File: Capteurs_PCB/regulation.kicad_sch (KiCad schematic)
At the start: 23 parts, among them U2 AZ1117-3.3

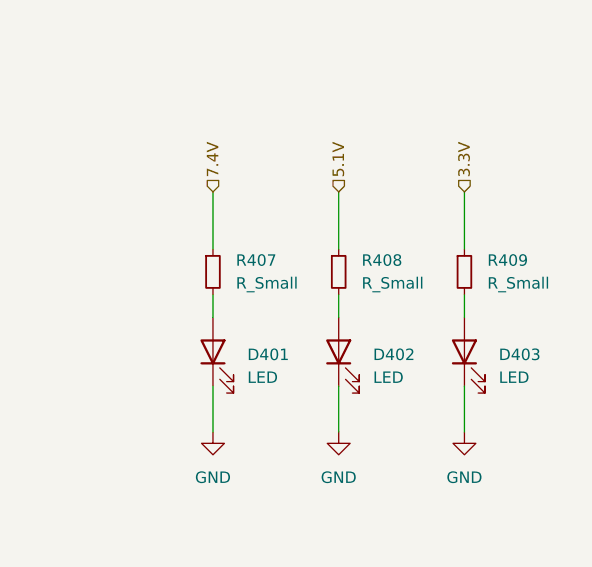
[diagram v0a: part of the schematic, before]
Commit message: Empreintes
A revoir car pas sur pour certaines + faire celles des composants modifiés
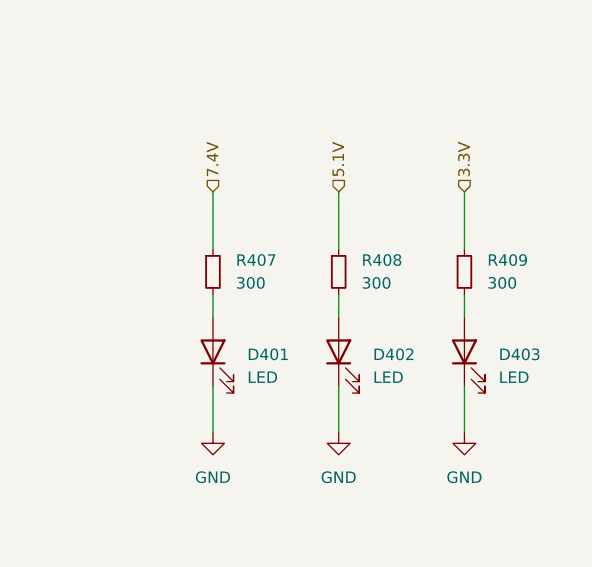
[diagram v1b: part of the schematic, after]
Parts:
- D401, D402, D403: footprint (none) -> LED_THT:LED_D5.0mm_Clear
- R1, R2, R401, R402, R403, R404: footprint (none) -> Resistor_SMD:R_0805_2012Metric
- R407, R408, R409: value R_Small -> 300; footprint (none) -> Resistor_SMD:R_0805_2012Metric
- U2: footprint (none) -> Package_TO_SOT_THT:TO-220-3_Vertical
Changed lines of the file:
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@@
       (effects (font (size 1.27 1.27)))
     )
-    (property "Footprint" "" (at 69.85 113.03 0)
+    (property "Footprint" "Resistor_SMD:R_0805_2012Metric" (at 69.85 113.03 0)
       (effects (font (size 1.27 1.27)) hide)
     )
@@
       (effects (font (size 1.27 1.27)) (justify left))
     )
-    (property "Footprint" "" (at 104.14 116.84 0)
+    (property "Footprint" "Resistor_SMD:R_0805_2012Metric" (at 104.14 116.84 0)
       (effects (font (size 1.27 1.27)) hide)
     )
@@
       (effects (font (size 1.27 1.27)) (justify right))
     )
-    (property "Footprint" "" (at 199.39 82.55 0)
+    (property "Footprint" "LED_THT:LED_D5.0mm_Clear" (at 199.39 82.55 0)
       (effects (font (size 1.27 1.27)) hide)
     )
@@
       (effects (font (size 1.27 1.27)) (justify right))
     )
-    (property "Footprint" "" (at 185.42 82.55 0)
+    (property "Footprint" "LED_THT:LED_D5.0mm_Clear" (at 185.42 82.55 0)
       (effects (font (size 1.27 1.27)) hide)
     )
@@
       (effects (font (size 1.27 1.27)) (justify left))
     )
-    (property "Value" "R_Small" (at 215.9 74.93 0)
-      (effects (font (size 1.27 1.27)) (justify left))
-    )
-    (property "Footprint" "" (at 213.36 73.66 0)
+    (property "Value" "300" (at 215.9 74.93 0)
+      (effects (font (size 1.27 1.27)) (justify left))
+    )
+    (property "Footprint" "Resistor_SMD:R_0805_2012Metric" (at 213.36 73.66 0)
       (effects (font (size 1.27 1.27)) hide)
     )
@@
       (effects (font (size 1.27 1.27)))
     )
-    (property "Footprint" "" (at 69.85 67.31 0)
+    (property "Footprint" "Resistor_SMD:R_0805_2012Metric" (at 69.85 67.31 0)
       (effects (font (size 1.27 1.27)) hide)
     )
@@
       (effects (font (size 1.27 1.27)) (justify left))
     )
-    (property "Value" "R_Small" (at 201.93 74.93 0)
-      (effects (font (size 1.27 1.27)) (justify left))
-    )
-    (property "Footprint" "" (at 199.39 73.66 0)
+    (property "Value" "300" (at 201.93 74.93 0)
+      (effects (font (size 1.27 1.27)) (justify left))
+    )
+    (property "Footprint" "Resistor_SMD:R_0805_2012Metric" (at 199.39 73.66 0)
       (effects (font (size 1.27 1.27)) hide)
     )
@@
       (effects (font (size 1.27 1.27)) (justify left))
     )
-    (property "Footprint" "" (at 104.14 109.22 0)
+    (property "Footprint" "Resistor_SMD:R_0805_2012Metric" (at 104.14 109.22 0)
       (effects (font (size 1.27 1.27)) hide)
     )
@@
       (effects (font (size 1.27 1.27)) (justify right))
     )
-    (property "Footprint" "" (at 213.36 82.55 0)
+    (property "Footprint" "LED_THT:LED_D5.0mm_Clear" (at 213.36 82.55 0)
       (effects (font (size 1.27 1.27)) hide)
     )
@@
       (effects (font (size 1.27 1.27)))
     )
-    (property "Footprint" "" (at 86.36 140.97 0)
+    (property "Footprint" "Package_TO_SOT_THT:TO-220-3_Vertical" (at 86.36 140.97 0)
       (effects (font (size 1.27 1.27) italic) hide)
     )
@@
       (effects (font (size 1.27 1.27)) (justify left))
     )
-    (property "Value" "R_Small" (at 187.96 74.93 0)
-      (effects (font (size 1.27 1.27)) (justify left))
-    )
-    (property "Footprint" "" (at 185.42 73.66 0)
+    (property "Value" "300" (at 187.96 74.93 0)
+      (effects (font (size 1.27 1.27)) (justify left))
+    )
+    (property "Footprint" "Resistor_SMD:R_0805_2012Metric" (at 185.42 73.66 0)
       (effects (font (size 1.27 1.27)) hide)
     )
@@
       (effects (font (size 1.27 1.27)) (justify left))
     )
-    (property "Footprint" "" (at 104.14 63.5 0)
+    (property "Footprint" "Resistor_SMD:R_0805_2012Metric" (at 104.14 63.5 0)
       (effects (font (size 1.27 1.27)) hide)
     )
@@
       (effects (font (size 1.27 1.27)) (justify left))
     )
-    (property "Footprint" "" (at 104.14 71.12 0)
-      (effects (font (size 1.27 1.27)) hide)
-    )
+    (property "Footprint" "Resistor_SMD:R_0805_2012Metric" (at 104.14 71.12 0)
+      (effects (font (size 1.27 1.27)) hide)
+    )

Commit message: Empreintes modifiées
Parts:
- C401, C405, C407, C408: footprint Capacitor_SMD:C_1206_3216Metric -> Capacitor_SMD:C_1206_3216Metric_Pad1.33x1.80mm_HandSolder
- R1, R2, R401, R402, R403, R404, R407, R408, R409: footprint Resistor_SMD:R_0805_2012Metric -> Resistor_SMD:R_0603_1608Metric_Pad0.98x0.95mm_HandSolder
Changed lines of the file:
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@@
       (effects (font (size 1.27 1.27)))
     )
-    (property "Footprint" "Resistor_SMD:R_0805_2012Metric" (at 69.85 113.03 0)
+    (property "Footprint" "Resistor_SMD:R_0603_1608Metric_Pad0.98x0.95mm_HandSolder" (at 69.85 113.03 0)
       (effects (font (size 1.27 1.27)) hide)
     )
@@
       (effects (font (size 1.27 1.27)) (justify left))
     )
-    (property "Footprint" "Resistor_SMD:R_0805_2012Metric" (at 104.14 116.84 0)
+    (property "Footprint" "Resistor_SMD:R_0603_1608Metric_Pad0.98x0.95mm_HandSolder" (at 104.14 116.84 0)
       (effects (font (size 1.27 1.27)) hide)
     )
@@
       (effects (font (size 1.27 1.27)))
     )
-    (property "Footprint" "Capacitor_SMD:C_1206_3216Metric" (at 69.85 69.85 0)
+    (property "Footprint" "Capacitor_SMD:C_1206_3216Metric_Pad1.33x1.80mm_HandSolder" (at 69.85 69.85 0)
       (effects (font (size 1.27 1.27)) hide)
     )
@@
       (effects (font (size 1.27 1.27)) (justify left))
     )
-    (property "Footprint" "Resistor_SMD:R_0805_2012Metric" (at 213.36 73.66 0)
+    (property "Footprint" "Resistor_SMD:R_0603_1608Metric_Pad0.98x0.95mm_HandSolder" (at 213.36 73.66 0)
       (effects (font (size 1.27 1.27)) hide)
     )
@@
       (effects (font (size 1.27 1.27)) (justify left))
     )
-    (property "Footprint" "Capacitor_SMD:C_1206_3216Metric" (at 104.14 152.4 0)
+    (property "Footprint" "Capacitor_SMD:C_1206_3216Metric_Pad1.33x1.80mm_HandSolder" (at 104.14 152.4 0)
       (effects (font (size 1.27 1.27)) hide)
     )
@@
       (effects (font (size 1.27 1.27)))
     )
-    (property "Footprint" "Resistor_SMD:R_0805_2012Metric" (at 69.85 67.31 0)
+    (property "Footprint" "Resistor_SMD:R_0603_1608Metric_Pad0.98x0.95mm_HandSolder" (at 69.85 67.31 0)
       (effects (font (size 1.27 1.27)) hide)
     )
@@
       (effects (font (size 1.27 1.27)) (justify left))
     )
-    (property "Footprint" "Resistor_SMD:R_0805_2012Metric" (at 199.39 73.66 0)
+    (property "Footprint" "Resistor_SMD:R_0603_1608Metric_Pad0.98x0.95mm_HandSolder" (at 199.39 73.66 0)
       (effects (font (size 1.27 1.27)) hide)
     )
@@
       (effects (font (size 1.27 1.27)) (justify left))
     )
-    (property "Footprint" "Resistor_SMD:R_0805_2012Metric" (at 104.14 109.22 0)
+    (property "Footprint" "Resistor_SMD:R_0603_1608Metric_Pad0.98x0.95mm_HandSolder" (at 104.14 109.22 0)
       (effects (font (size 1.27 1.27)) hide)
     )
@@
       (effects (font (size 1.27 1.27)) (justify left))
     )
-    (property "Footprint" "Capacitor_SMD:C_1206_3216Metric" (at 69.85 152.4 0)
+    (property "Footprint" "Capacitor_SMD:C_1206_3216Metric_Pad1.33x1.80mm_HandSolder" (at 69.85 152.4 0)
       (effects (font (size 1.27 1.27)) hide)
     )
@@
       (effects (font (size 1.27 1.27)) (justify left))
     )
-    (property "Footprint" "Resistor_SMD:R_0805_2012Metric" (at 185.42 73.66 0)
+    (property "Footprint" "Resistor_SMD:R_0603_1608Metric_Pad0.98x0.95mm_HandSolder" (at 185.42 73.66 0)
       (effects (font (size 1.27 1.27)) hide)
     )
@@
       (effects (font (size 1.27 1.27)) (justify left))
     )
-    (property "Footprint" "Resistor_SMD:R_0805_2012Metric" (at 104.14 63.5 0)
+    (property "Footprint" "Resistor_SMD:R_0603_1608Metric_Pad0.98x0.95mm_HandSolder" (at 104.14 63.5 0)
       (effects (font (size 1.27 1.27)) hide)
     )
@@
       (effects (font (size 1.27 1.27)) (justify left))
     )
-    (property "Footprint" "Resistor_SMD:R_0805_2012Metric" (at 104.14 71.12 0)
+    (property "Footprint" "Resistor_SMD:R_0603_1608Metric_Pad0.98x0.95mm_HandSolder" (at 104.14 71.12 0)
       (effects (font (size 1.27 1.27)) hide)
     )
@@
       (effects (font (size 1.27 1.27)))
     )
-    (property "Footprint" "Capacitor_SMD:C_1206_3216Metric" (at 69.85 115.57 0)
-      (effects (font (size 1.27 1.27)) hide)
-    )
+    (property "Footprint" "Capacitor_SMD:C_1206_3216Metric_Pad1.33x1.80mm_HandSolder" (at 69.85 115.57 0)
+      (effects (font (size 1.27 1.27)) hide)
+    )

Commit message: Footprint design and Footprint assignment
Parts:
- removed C407: 10u, Capacitor_SMD:C_1206_3216Metric_Pad1.33x1.80mm_HandSolder, symbol Device:C_Small
- removed C408: 22u, Capacitor_SMD:C_1206_3216Metric_Pad1.33x1.80mm_HandSolder, symbol Device:C_Small
- removed U2: AZ1117-3.3, Package_TO_SOT_THT:TO-220-3_Vertical, symbol Regulator_Linear:AZ1117-3.3
- added C5: 10u, Capacitor_SMD:CP_Elec_5x5.4, symbol Device:C_Polarized_Small
- added C8: 47u, Capacitor_SMD:CP_Elec_6.3x5.4, symbol Device:C_Polarized_Small
- added C9: 1u, Capacitor_SMD:C_1206_3216Metric_Pad1.33x1.80mm_HandSolder, symbol Device:C_Small
- added R3: 140, Resistor_SMD:R_0603_1608Metric_Pad0.98x0.95mm_HandSolder, symbol Device:R_Small
- added R4: 5.6k, Resistor_SMD:R_0603_1608Metric_Pad0.98x0.95mm_HandSolder, symbol Device:R_Small
- added R5: 402k, Resistor_SMD:R_0603_1608Metric_Pad0.98x0.95mm_HandSolder, symbol Device:R_Small
- added U2: ~, Custom:Regulator, symbol custom:171013801
- U401, U402: footprint (none) -> Custom:Regulator
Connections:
- net 3.3V: now also C8.1, R3.1, U2.6 (Vout)
- net GND: now also C5.2, C8.2, C9.1, R4.1, R5.2, U2.10 (AGND), U2.13 (PGND)
- net Vin: now also C5.1, U2.4 (Vin), U2.5 (Vin)
- new net: C9.2, U2.3 (Vcc)
- new net: R4.2, U2.1 (FSW)
- new net: U2.12 (En), U2.9 (Vin_link)
- new net: R3.2, R5.1, U2.2 (FB)
- no-connect marks 4 -> 6

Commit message: Routage en cours
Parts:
- C401, C405, C9: footprint Capacitor_SMD:C_1206_3216Metric_Pad1.33x1.80mm_HandSolder -> Capacitor_SMD:C_0603_1608Metric_Pad1.08x0.95mm_HandSolder
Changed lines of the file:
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@@
   (junction (at 104.14 67.31) (diameter 0) (color 0 0 0 0)
-  )
-  (junction (at 54.61 146.05) (diameter 0) (color 0 0 0 0)
   )
   (junction (at 71.12 146.05) (diameter 0) (color 0 0 0 0)
@@
     (stroke (width 0) (type default))
   )
-  (wire (pts (xy 54.61 146.05) (xy 57.15 146.05))
-    (stroke (width 0) (type default))
-  )
   (wire (pts (xy 62.23 118.11) (xy 62.23 115.57))
     (stroke (width 0) (type default))
@@
     (stroke (width 0) (type default))
   )
-  (wire (pts (xy 49.53 146.05) (xy 54.61 146.05))
+  (wire (pts (xy 49.53 146.05) (xy 57.15 146.05))
     (stroke (width 0) (type default))
   )
@@
       (effects (font (size 1.27 1.27)))
     )
-    (property "Footprint" "Capacitor_SMD:C_1206_3216Metric_Pad1.33x1.80mm_HandSolder" (at 69.85 163.83 0)
+    (property "Footprint" "Capacitor_SMD:C_0603_1608Metric_Pad1.08x0.95mm_HandSolder" (at 69.85 163.83 0)
       (effects (font (size 1.27 1.27)) hide)
     )
@@
       (effects (font (size 1.27 1.27)))
     )
-    (property "Footprint" "Capacitor_SMD:C_1206_3216Metric_Pad1.33x1.80mm_HandSolder" (at 69.85 69.85 0)
+    (property "Footprint" "Capacitor_SMD:C_0603_1608Metric_Pad1.08x0.95mm_HandSolder" (at 69.85 69.85 0)
       (effects (font (size 1.27 1.27)) hide)
     )
@@
     )
   )
-  (symbol (lib_id "power:PWR_FLAG") (at 54.61 146.05 0) (unit 1)
-    (in_bom yes) (on_board yes) (dnp no) (fields_autoplaced)
-    (property "Reference" "#FLG06" (at 54.61 144.145 0)
-      (effects (font (size 1.27 1.27)) hide)
-    )
-    (property "Value" "PWR_FLAG" (at 54.61 142.24 0)
-      (effects (font (size 1.27 1.27)))
-    )
-    (property "Footprint" "" (at 54.61 146.05 0)
-      (effects (font (size 1.27 1.27)) hide)
-    )
-    (property "Datasheet" "~" (at 54.61 146.05 0)
-      (effects (font (size 1.27 1.27)) hide)
-    )
-    (pin "1")
-    (instances
-      (project "Capteurs_PCB"
-        (path "/1101af8f-9425-4102-9245-339dc54562bf/b84a61ef-89d4-47b7-a16e-5e36daa53b0c"
-          (reference "#FLG06") (unit 1)
-        )
-      )
-    )
-  )
   (symbol (lib_id "power:GND") (at 87.63 130.81 0) (unit 1)
     (in_bom yes) (on_board yes) (dnp no) (fields_autoplaced)
@@
       (effects (font (size 1.27 1.27)))
     )
-    (property "Footprint" "Capacitor_SMD:C_1206_3216Metric_Pad1.33x1.80mm_HandSolder" (at 69.85 115.57 0)
-      (effects (font (size 1.27 1.27)) hide)
-    )
+    (property "Footprint" "Capacitor_SMD:C_0603_1608Metric_Pad1.08x0.95mm_HandSolder" (at 69.85 115.57 0)
+      (effects (font (size 1.27 1.27)) hide)
+    )

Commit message: Début de routage
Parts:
- D401, D402, D403: footprint LED_THT:LED_D5.0mm_Clear -> LED_SMD:LED_0402_1005Metric_Pad0.77x0.64mm_HandSolder
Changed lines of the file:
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@@
       (effects (font (size 1.27 1.27)) (justify right))
     )
-    (property "Footprint" "LED_THT:LED_D5.0mm_Clear" (at 199.39 82.55 0)
+    (property "Footprint" "LED_SMD:LED_0402_1005Metric_Pad0.77x0.64mm_HandSolder" (at 199.39 82.55 0)
       (effects (font (size 1.27 1.27)) hide)
     )
@@
       (effects (font (size 1.27 1.27)) (justify right))
     )
-    (property "Footprint" "LED_THT:LED_D5.0mm_Clear" (at 185.42 82.55 0)
+    (property "Footprint" "LED_SMD:LED_0402_1005Metric_Pad0.77x0.64mm_HandSolder" (at 185.42 82.55 0)
       (effects (font (size 1.27 1.27)) hide)
     )
@@
       (effects (font (size 1.27 1.27)) (justify right))
     )
-    (property "Footprint" "LED_THT:LED_D5.0mm_Clear" (at 213.36 82.55 0)
-      (effects (font (size 1.27 1.27)) hide)
-    )
+    (property "Footprint" "LED_SMD:LED_0402_1005Metric_Pad0.77x0.64mm_HandSolder" (at 213.36 82.55 0)
+      (effects (font (size 1.27 1.27)) hide)
+    )

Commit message: Problème réglé
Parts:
- R1: value 402k -> 30.1k
- R2: value 52.2k -> 402k
- R3: value 140 -> 402k
- R402: value 80.4 -> 402k
- R403: value 402k -> 80.4k
- R5: value 402k -> 140k
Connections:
- net 7.4V: no longer C406.1, R2.1, U402.6 (Vout)
- new net 12V: C406.1, R2.1, U402.6 (Vout)
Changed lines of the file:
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@@
     (effects (font (size 1.27 1.27)) (justify right))
   )
-  (hierarchical_label "7.4V" (shape input) (at 132.08 52.07 0) (fields_autoplaced)
+  (hierarchical_label "12V" (shape input) (at 132.08 52.07 0) (fields_autoplaced)
     (effects (font (size 1.27 1.27)) (justify left))
   )
@@
       (effects (font (size 1.27 1.27)) (justify left))
     )
-    (property "Value" "402k" (at 106.68 118.745 0)
+    (property "Value" "80.4k" (at 106.68 118.745 0)
       (effects (font (size 1.27 1.27)) (justify left))
     )
@@
       (effects (font (size 1.27 1.27)) (justify left))
     )
-    (property "Value" "80.4" (at 106.68 111.125 0)
+    (property "Value" "402k" (at 106.68 111.125 0)
       (effects (font (size 1.27 1.27)) (justify left))
     )
@@
       (effects (font (size 1.27 1.27)) (justify left))
     )
-    (property "Value" "52.2k" (at 106.68 65.405 0)
+    (property "Value" "402k" (at 106.68 65.405 0)
       (effects (font (size 1.27 1.27)) (justify left))
     )
@@
       (effects (font (size 1.27 1.27)) (justify left))
     )
-    (property "Value" "402k" (at 106.68 73.025 0)
+    (property "Value" "30.1k" (at 106.68 73.025 0)
       (effects (font (size 1.27 1.27)) (justify left))
     )
@@
       (effects (font (size 1.27 1.27)) (justify left))
     )
-    (property "Value" "402k" (at 106.68 167.005 0)
+    (property "Value" "140k" (at 106.68 167.005 0)
       (effects (font (size 1.27 1.27)) (justify left))
     )
@@
       (effects (font (size 1.27 1.27)) (justify left))
     )
-    (property "Value" "140" (at 106.68 159.385 0)
-      (effects (font (size 1.27 1.27)) (justify left))
-    )
+    (property "Value" "402k" (at 106.68 159.385 0)
+      (effects (font (size 1.27 1.27)) (justify left))
+    )

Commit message: modifs kicad
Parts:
- R1: value 30.1k -> 52.2k
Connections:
- net 12V renamed 7.5V
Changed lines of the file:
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@@
     (effects (font (size 1.27 1.27)) (justify right))
   )
-  (hierarchical_label "12V" (shape input) (at 132.08 52.07 0) (fields_autoplaced)
+  (hierarchical_label "7.5V" (shape input) (at 132.08 52.07 0) (fields_autoplaced)
     (effects (font (size 1.27 1.27)) (justify left))
   )
@@
       (effects (font (size 1.27 1.27)) (justify left))
     )
-    (property "Value" "30.1k" (at 106.68 73.025 0)
-      (effects (font (size 1.27 1.27)) (justify left))
-    )
+    (property "Value" "52.2k" (at 106.68 73.025 0)
+      (effects (font (size 1.27 1.27)) (justify left))
+    )
